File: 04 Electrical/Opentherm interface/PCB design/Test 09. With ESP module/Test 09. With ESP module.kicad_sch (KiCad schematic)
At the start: 31 parts, among them J1 OpenTherm, J2 Laser range sensor, J3 ST7789, J4 Encoder, J5 Encoder, Q1 MMBT2907A, SW1 RotaryEncoder_Switch, U1 DS18S20, U2 DS18S20, U3 DS18S20, U4 DS18S20, U5 EL357N-G, U6 EL357N-G, U7 mini_esp32

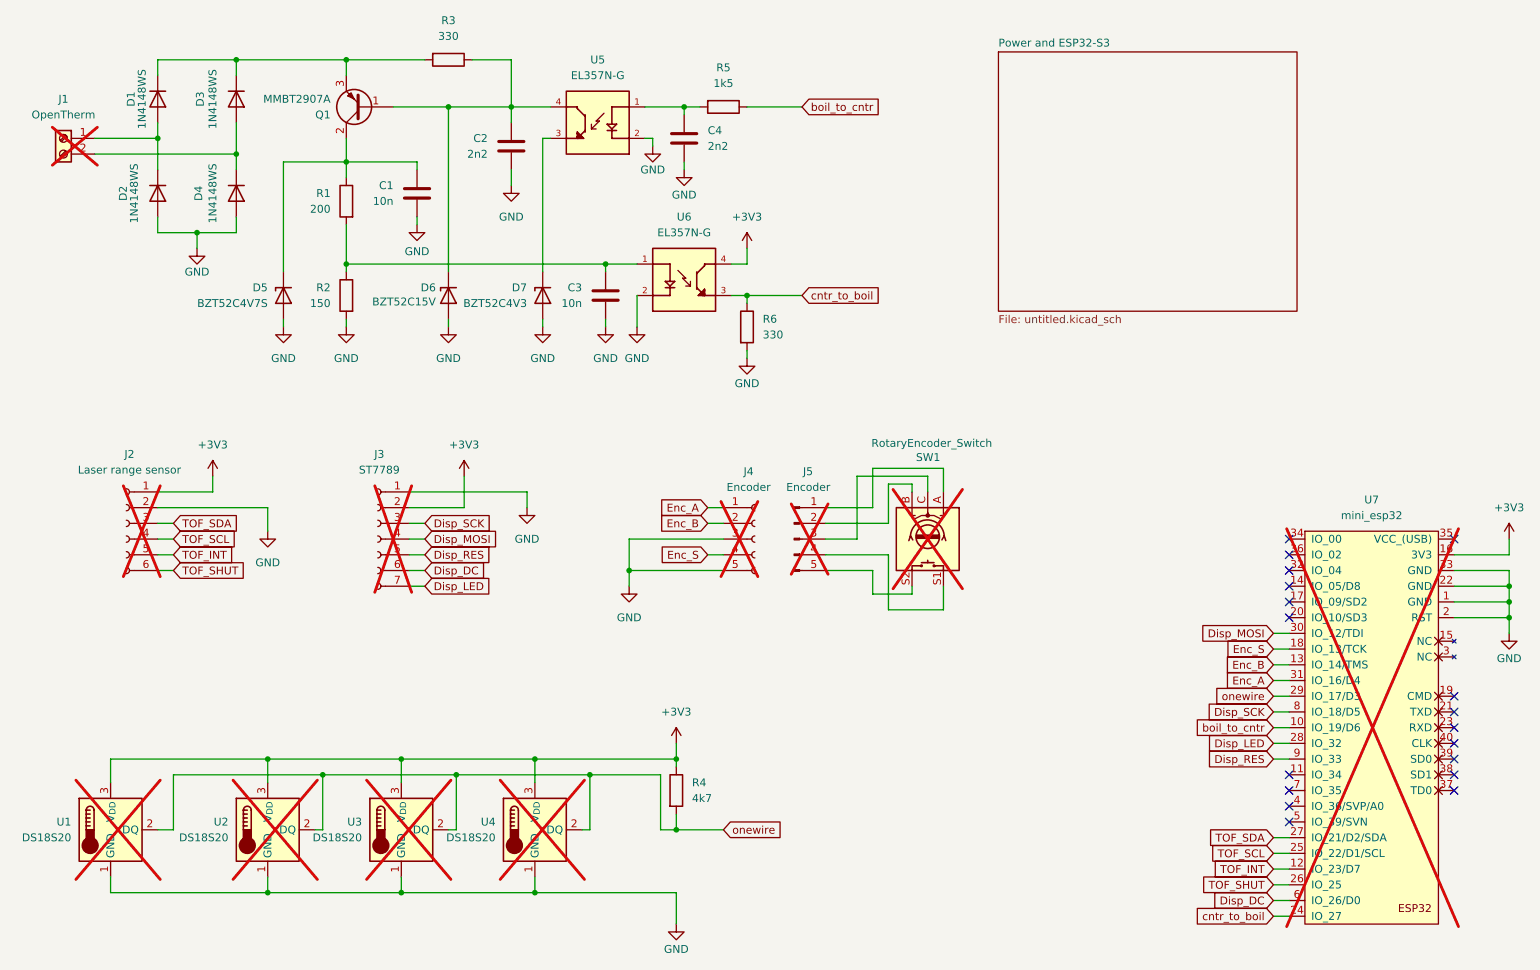
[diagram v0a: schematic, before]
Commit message: First version of PCB without errors
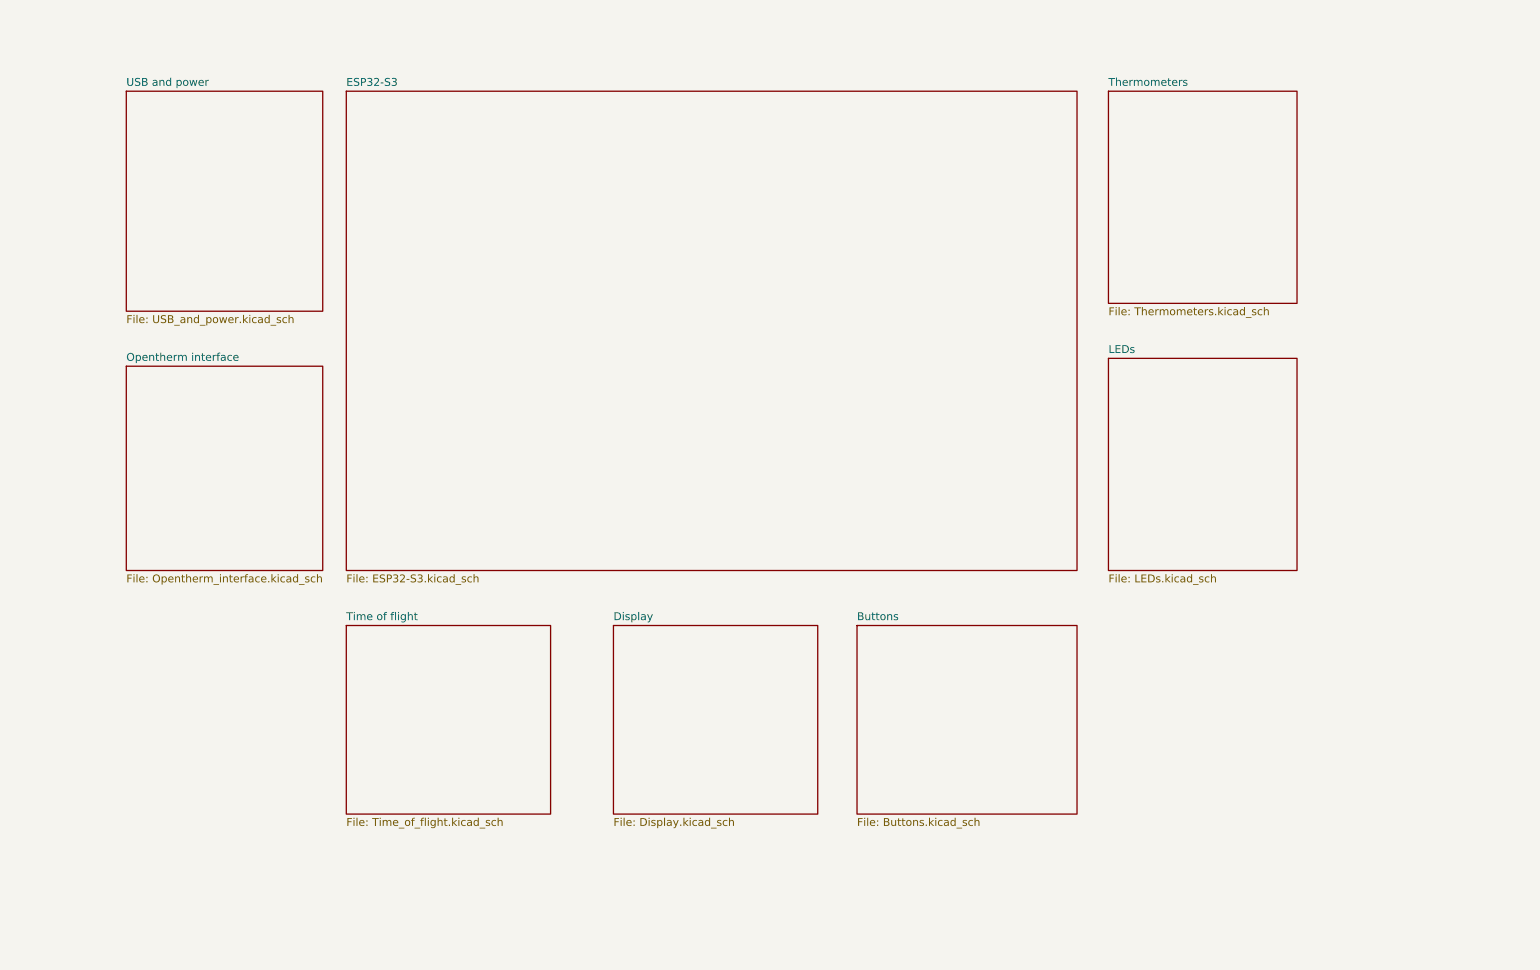
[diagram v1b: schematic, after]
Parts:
- removed C1, C3: 10n, Capacitor_SMD:C_0603_1608Metric, symbol Device:C
- removed C2, C4: 2n2, Capacitor_SMD:C_0603_1608Metric, symbol Device:C
- removed D1, D2, D3, D4: 1N4148WS, Diode_SMD:D_SOD-323, symbol Simulation_SPICE:D
- removed D5: BZT52C4V7S, Diode_SMD:D_SOD-323, symbol Device:D_Zener
- removed D6: BZT52C15V, Diode_SMD:D_SOD-123, symbol Device:D_Zener
- removed D7: BZT52C4V3, Diode_SMD:D_SOD-123, symbol Device:D_Zener
- removed J1: OpenTherm, TerminalBlock:TerminalBlock_bornier-2_P5.08mm, symbol Connector:Screw_Terminal_01x02
- removed J2: Laser range sensor, Connector_PinHeader_2.54mm:PinHeader_1x06_P2.54mm_Vertical, symbol Connector:Conn_01x06_Socket
- removed J3: ST7789, Connector_PinHeader_2.54mm:PinHeader_1x07_P2.54mm_Vertical, symbol Connector:Conn_01x07_Socket
- removed J4: Encoder, Connector_PinHeader_2.54mm:PinHeader_1x05_P2.54mm_Vertical, symbol Connector:Conn_01x05_Socket
- removed J5: Encoder, symbol Connector:Conn_01x05_Pin
- removed Q1: MMBT2907A, Package_TO_SOT_SMD:SOT-23, symbol Device:Q_PNP_BCE
- removed R1: 200, Resistor_SMD:R_0805_2012Metric, symbol Device:R
- removed R2: 150, Resistor_SMD:R_0805_2012Metric, symbol Device:R
- removed R3: 330, Resistor_SMD:R_0805_2012Metric, symbol Device:R
- removed R4: 4k7, Resistor_SMD:R_0805_2012Metric, symbol Device:R
- removed R5: 1k5, Diode_SMD:D_0805_2012Metric, symbol Device:R
- removed R6: 330, Diode_SMD:D_0805_2012Metric, symbol Device:R
- removed SW1: RotaryEncoder_Switch, symbol Device:RotaryEncoder_Switch
- removed U1, U2, U3, U4: DS18S20, Package_TO_SOT_THT:TO-92L_HandSolder, symbol Sensor_Temperature:DS18S20
- removed U5, U6: EL357N-G, EL357N-G:OPTO_EL357N-G, symbol EL357N-G:EL357N-G
- removed U7: mini_esp32, ESP32_mini:ESP32_mini, symbol ESP32_mini:mini_esp32
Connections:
- no-connect marks 18 -> 0
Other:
- sheet Power and ESP32-S3 renamed ESP32-S3
- added sheet Buttons (Buttons.kicad_sch)
- added sheet Display (Display.kicad_sch)
- added sheet LEDs (LEDs.kicad_sch)
- added sheet Opentherm interface (Opentherm_interface.kicad_sch)
- added sheet Thermometers (Thermometers.kicad_sch)
- added sheet Time of flight (Time_of_flight.kicad_sch)
- added sheet USB and power (USB_and_power.kicad_sch)
- sheet ESP32-S3: file untitled.kicad_sch -> ESP32-S3.kicad_sch

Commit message: Schematic update
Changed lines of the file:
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@@
 	(generator_version "8.0")
 	(paper "A4")
+	(polyline
+		(pts
+			(xy 74.93 88.9) (xy 80.01 88.9)
+		)
+		(stroke
+			(width 0)
+			(type default)
+		)
+	)
+	(polyline
+		(pts
+			(xy 74.93 48.26) (xy 80.01 48.26)
+		)
+		(stroke
+			(width 0)
+			(type default)
+		)
+	)
+	(polyline
+		(pts
+			(xy 180.34 114.3) (xy 180.34 105.41)
+		)
+		(stroke
+			(width 0)
+			(type default)
+		)
+	)
+	(polyline
+		(pts
+			(xy 198.12 88.9) (xy 203.2 88.9)
+		)
+		(stroke
+			(width 0)
+			(type default)
+		)
+	)
+	(polyline
+		(pts
+			(xy 139.7 114.3) (xy 139.7 105.41)
+		)
+		(stroke
+			(width 0)
+			(type default)
+		)
+	)
+	(polyline
+		(pts
+			(xy 96.52 114.3) (xy 96.52 105.41)
+		)
+		(stroke
+			(width 0)
+			(type default)
+		)
+	)
+	(polyline
+		(pts
+			(xy 198.12 44.45) (xy 203.2 44.45)
+		)
+		(stroke
+			(width 0)
+			(type default)
+		)
+	)
 	(sheet
 		(at 203.2 27.94)
@@
 	)
 	(sheet
-		(at 44.45 27.94)
+		(at 43.18 27.94)
 		(size 31.75 35.56)
 		(fields_autoplaced yes)
@@
 		)
 		(property "Sheetname" "USB and power"
-			(at 44.45 27.2284 0)
+			(at 43.18 27.2284 0)
 			(effects
 				(font
@@
 		)
 		(property "Sheetfile" "USB_and_power.kicad_sch"
-			(at 44.45 64.0846 0)
+			(at 43.18 64.0846 0)
 			(effects
 				(font
@@
 	)
 	(sheet
-		(at 44.45 72.39)
+		(at 43.18 72.39)
 		(size 31.75 33.02)
 		(fields_autoplaced yes)
@@
 		)
 		(property "Sheetname" "Opentherm interface"
-			(at 44.45 71.6784 0)
+			(at 43.18 71.6784 0)
 			(effects
 				(font
@@
 		)
 		(property "Sheetfile" "Opentherm_interface.kicad_sch"
-			(at 44.45 105.9946 0)
-			(effects
-				(font
+			(at 43.18 105.9946 0)
+			(effects
+				(font
